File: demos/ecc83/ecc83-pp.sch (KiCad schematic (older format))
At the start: 15 parts, among them P1 IN, P2 OUT, P3 POWER, P4 CONN_2, P5 CONN_1, P6 CONN_1, P7 CONN_1, P8 CONN_1, U1 ECC83

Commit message: Update demos to use sym-lib-table and recent libraries
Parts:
- C1, C2: symbol C -> ecc83_schlib:C
- P1, P2, P3, P4: symbol CONN_2 -> ecc83_schlib:CONN_2
- P5, P6, P7, P8: symbol CONN_1 -> ecc83_schlib:CONN_1
- R1, R2, R3, R4: symbol R -> ecc83_schlib:R
- U1: symbol ECC83 -> ecc83_schlib:ECC83
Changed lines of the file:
@@
-EESchema Schematic File Version 2
-LIBS:ecc83_schlib
-EELAYER 25 0
+EESchema Schematic File Version 4
+LIBS:ecc83-pp-cache
+EELAYER 26 0
 EELAYER END
 $Descr A4 11693 8268
@@
 	6200 3500 6200 3850
 $Comp
-L ECC83 U1
+L ecc83_schlib:ECC83 U1
 U 3 1 48B4F266
 P 2500 2950
@@
 $EndComp
 $Comp
-L ECC83 U1
+L ecc83_schlib:ECC83 U1
 U 2 1 48B4F263
 P 6200 4250
@@
 $EndComp
 $Comp
-L ECC83 U1
+L ecc83_schlib:ECC83 U1
 U 1 1 48B4F256
 P 6300 2550
@@
 $EndComp
 $Comp
-L GND #PWR01
+L ecc83_schlib:GND #PWR01
 U 1 1 457DBAF8
 P 7700 3300
@@
 $EndComp
 $Comp
-L GND #PWR02
+L ecc83_schlib:GND #PWR02
 U 1 1 457DBAF5
 P 7300 3550
@@
 $EndComp
 $Comp
-L GND #PWR03
+L ecc83_schlib:GND #PWR03
 U 1 1 457DBAF1
 P 6100 5200
@@
 $EndComp
 $Comp
-L GND #PWR04
+L ecc83_schlib:GND #PWR04
 U 1 1 457DBAEF
 P 5700 5200
@@
 $EndComp
 $Comp
-L PWR_FLAG #FLG05
+L ecc83_schlib:PWR_FLAG #FLG05
 U 1 1 457DBAC0
 P 3000 2350
@@
 $EndComp
 $Comp
-L CONN_2 P4
+L ecc83_schlib:CONN_2 P4
 U 1 1 456A8ACC
 P 1650 3600
@@
 $EndComp
 $Comp
-L C C1
+L ecc83_schlib:C C1
 U 1 1 4549F4BE
 P 3400 2250
@@
 $EndComp
 $Comp
-L CONN_2 P3
+L ecc83_schlib:CONN_2 P3
 U 1 1 4549F4A5
 P 1650 2100
@@
 $EndComp
 $Comp
-L CONN_2 P2
+L ecc83_schlib:CONN_2 P2
 U 1 1 4549F46C
 P 8150 3100
@@
 $EndComp
 $Comp
-L CONN_2 P1
+L ecc83_schlib:CONN_2 P1
 U 1 1 4549F464
 P 5000 4350
@@
 $EndComp
 $Comp
-L C C2
+L ecc83_schlib:C C2
 U 1 1 4549F3BE
 P 6900 3000
@@
 $EndComp
 $Comp
-L R R3
+L ecc83_schlib:R R3
 U 1 1 4549F3AD
 P 7300 3350
@@
 $EndComp
 $Comp
-L R R4
+L ecc83_schlib:R R4
 U 1 1 4549F3A2
 P 5700 5000
@@
 $EndComp
 $Comp
-L R R2
+L ecc83_schlib:R R2
 U 1 1 4549F39D
 P 6100 5000
@@
 $EndComp
 $Comp
-L R R1
+L ecc83_schlib:R R1
 U 1 1 4549F38A
 P 6200 3350
@@
 $EndComp
 $Comp
-L GND #PWR06
+L ecc83_schlib:GND #PWR06
 U 1 1 53B6F370
 P 3400 2450
@@
 $EndComp
 $Comp
-L CONN_1 P5
+L ecc83_schlib:CONN_1 P5
 U 1 1 54A5890A
 P 6250 7000
@@
 $EndComp
 $Comp
-L CONN_1 P6
+L ecc83_schlib:CONN_1 P6
 U 1 1 54A58C65
 P 6250 7100
@@
 $EndComp
 $Comp
-L CONN_1 P7
+L ecc83_schlib:CONN_1 P7
 U 1 1 54A58C8A
 P 6250 7200
@@
 $EndComp
 $Comp
-L CONN_1 P8
+L ecc83_schlib:CONN_1 P8
 U 1 1 54A58CA3
 P 6250 7300
@@
 	3400 2450 3400 2400
 $Comp
-L PWR_FLAG #FLG07
+L ecc83_schlib:PWR_FLAG #FLG07
 U 1 1 550EA992
 P 3000 1950
@@
 Connection ~ 3000 2000
 $Comp
-L GND #PWR08
+L ecc83_schlib:GND #PWR08
 U 1 1 550EAB37
 P 3000 2550
@@
 Connection ~ 3000 2450
 $Comp
-L GND #PWR09
+L ecc83_schlib:GND #PWR09
 U 1 1 550EAF5A
 P 5450 4600

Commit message: update demo ecc83
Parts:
- C1: symbol ecc83_schlib:C -> ecc83_schlib:CP
- P1, P2, P3, P4: footprint connect:bornier2 -> TerminalBlock_Phoenix:TerminalBlock_Phoenix_MKDS-1,5-2_1x02_P5.00mm_Horizontal
- U1: footprint Valves:VALVE-ECC-83-1 -> Valve:Valve_ECC-83-1
- U1: footprint Valves:VALVE-ECC-83-1 -> (none)
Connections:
- net at U1.4 (F1), U1.5 (F1): now also P4.2 (PM); no longer P4.1 (P1)
- net at U1.9 (F2): now also P4.1 (P1); no longer P4.2 (PM)
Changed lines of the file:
@@
 	6100 4650 6100 4850
 Wire Wire Line
-	2000 2000 6300 2000
+	2000 2000 3000 2000
 Connection ~ 3400 2000
 Wire Wire Line
-	7050 3000 7800 3000
+	7050 3000 7300 3000
 Wire Wire Line
 	7300 3000 7300 3200
 Wire Wire Line
-	2000 3500 2600 3500
+	2000 3500 2400 3500
 Wire Wire Line
 	2400 3500 2400 3400
 Wire Wire Line
-	6200 3500 6200 3850
+	6200 3500 6200 3700
 $Comp
 L ecc83_schlib:ECC83 U1
@@
 F 0 "U1" H 2500 3400 50  0000 C CNN
 F 1 "ECC83" H 2500 3300 50  0000 C CNN
-F 2 "Valves:VALVE-ECC-83-1" V 2250 2950 30  0000 C CNN
+F 2 "" V 2250 2950 30  0000 C CNN
 F 3 "" H 2500 2950 60  0001 C CNN
 	3    2500 2950
@@
 F 0 "U1" H 6350 4600 50  0000 C CNN
 F 1 "ECC83" H 6400 3900 50  0000 C CNN
-F 2 "Valves:VALVE-ECC-83-1" H 6400 3850 30  0000 C CNN
+F 2 "" H 6400 3850 30  0000 C CNN
 F 3 "" H 6200 4250 60  0001 C CNN
 	2    6200 4250
@@
 F 0 "U1" H 6450 2900 50  0000 C CNN
 F 1 "ECC83" H 6050 2250 50  0000 C CNN
-F 2 "Valves:VALVE-ECC-83-1" H 6570 2150 50  0001 C CNN
+F 2 "Valve:Valve_ECC-83-1" V 6550 2550 30  0000 C CNN
 F 3 "" H 6300 2550 60  0001 C CNN
 	1    6300 2550
@@
 L ecc83_schlib:PWR_FLAG #FLG05
 U 1 1 457DBAC0
-P 3000 2350
-F 0 "#FLG05" H 3000 2620 30  0001 C CNN
-F 1 "PWR_FLAG" H 3000 2580 30  0000 C CNN
-F 2 "" H 3000 2350 60  0001 C CNN
-F 3 "" H 3000 2350 60  0001 C CNN
-	1    3000 2350
-	1    0    0    -1
+P 2100 2200
+F 0 "#FLG05" H 2100 2470 30  0001 C CNN
+F 1 "PWR_FLAG" H 2100 2430 30  0000 C CNN
+F 2 "" H 2100 2200 60  0001 C CNN
+F 3 "" H 2100 2200 60  0001 C CNN
+	1    2100 2200
+	0    1    1    0
 $EndComp
 $Comp
@@
 F 0 "P4" V 1600 3600 40  0000 C CNN
 F 1 "CONN_2" V 1700 3600 40  0000 C CNN
-F 2 "connect:bornier2" H 1650 3600 60  0001 C CNN
+F 2 "TerminalBlock_Phoenix:TerminalBlock_Phoenix_MKDS-1,5-2_1x02_P5.00mm_Horizontal" H 1600 3800 15  0000 C CNN
 F 3 "" H 1650 3600 60  0001 C CNN
 	1    1650 3600
-	-1   0    0    -1
-$EndComp
-$Comp
-L ecc83_schlib:C C1
+	-1   0    0    1
+$EndComp
+$Comp
+L ecc83_schlib:CP C1
 U 1 1 4549F4BE
 P 3400 2250
-F 0 "C1" H 3450 2350 50  0000 L CNN
-F 1 "10uF" H 3150 2350 50  0000 L CNN
-F 2 "discret:C2V10" H 3400 2250 60  0001 C CNN
+F 0 "C1" H 3150 2300 50  0000 L CNN
+F 1 "10uF" H 3100 2200 50  0000 L CNN
+F 2 "discret:C2V10" H 3200 2150 30  0000 C CNN
 F 3 "" H 3400 2250 60  0001 C CNN
 	1    3400 2250
@@
 U 1 1 4549F4A5
 P 1650 2100
-F 0 "P3" V 1600 2100 40  0000 C CNN
+F 0 "P3" H 1650 2300 40  0000 C CNN
 F 1 "POWER" V 1700 2100 40  0000 C CNN
-F 2 "connect:bornier2" H 1650 2100 60  0001 C CNN
+F 2 "TerminalBlock_Phoenix:TerminalBlock_Phoenix_MKDS-1,5-2_1x02_P5.00mm_Horizontal" H 1650 1900 15  0000 C CNN
 F 3 "" H 1650 2100 60  0001 C CNN
 	1    1650 2100
@@
 U 1 1 4549F46C
 P 8150 3100
-F 0 "P2" V 8100 3100 40  0000 C CNN
+F 0 "P2" H 8150 3300 40  0000 C CNN
 F 1 "OUT" V 8200 3100 40  0000 C CNN
-F 2 "connect:bornier2" H 8150 3100 60  0001 C CNN
+F 2 "TerminalBlock_Phoenix:TerminalBlock_Phoenix_MKDS-1,5-2_1x02_P5.00mm_Horizontal" H 8150 2900 15  0000 C CNN
 F 3 "" H 8150 3100 60  0001 C CNN
 	1    8150 3100
@@
 U 1 1 4549F464
 P 5000 4350
-F 0 "P1" V 4950 4350 40  0000 C CNN
-F 1 "IN" V 5050 4350 40  0000 C CNN
-F 2 "connect:bornier2" H 5000 4600 50  0000 C CNN
+F 0 "P1" H 5000 4150 40  0000 C CNN
+F 1 "IN" H 5000 4350 40  0000 C CNN
+F 2 "TerminalBlock_Phoenix:TerminalBlock_Phoenix_MKDS-1,5-2_1x02_P5.00mm_Horizontal" H 5000 4550 15  0000 C CNN
 F 3 "" H 5000 4350 60  0001 C CNN
 	1    5000 4350
@@
 F 0 "C2" V 6750 3000 50  0000 C CNN
 F 1 "680nF" V 7050 3000 50  0000 C CNN
-F 2 "discret:C2" H 6900 3000 60  0001 C CNN
+F 2 "discret:C2" V 7100 3000 30  0000 C CNN
 F 3 "" H 6900 3000 60  0001 C CNN
 	1    6900 3000
@@
 U 1 1 4549F3AD
 P 7300 3350
-F 0 "R3" H 7200 3550 50  0000 C CNN
+F 0 "R3" H 7200 3350 50  0000 C CNN
 F 1 "100K" V 7300 3350 50  0000 C CNN
-F 2 "discret:R3" H 7300 3350 60  0001 C CNN
+F 2 "discret:R3" V 7379 3350 30  0000 C CNN
 F 3 "" H 7300 3350 60  0001 C CNN
 	1    7300 3350
@@
 U 1 1 4549F3A2
 P 5700 5000
-F 0 "R4" H 5600 5200 50  0000 C CNN
+F 0 "R4" H 5600 5050 50  0000 C CNN
 F 1 "47K" V 5700 5000 50  0000 C CNN
-F 2 "discret:R3" H 5700 5000 60  0001 C CNN
+F 2 "discret:R3" V 5776 4998 30  0000 C CNN
 F 3 "" H 5700 5000 60  0001 C CNN
 	1    5700 5000
@@
 U 1 1 4549F39D
 P 6100 5000
-F 0 "R2" H 6000 5200 50  0000 C CNN
+F 0 "R2" H 6000 5000 50  0000 C CNN
 F 1 "1.5K" V 6100 5000 50  0000 C CNN
-F 2 "discret:R3" H 6100 5000 60  0001 C CNN
+F 2 "discret:R3" V 6174 5000 30  0000 C CNN
 F 3 "" H 6100 5000 60  0001 C CNN
 	1    6100 5000
@@
 U 1 1 4549F38A
 P 6200 3350
-F 0 "R1" H 6300 3150 50  0000 C CNN
+F 0 "R1" H 6300 3350 50  0000 C CNN
 F 1 "1.5K" V 6200 3350 50  0000 C CNN
-F 2 "discret:R3" H 6200 3350 60  0001 C CNN
+F 2 "discret:R3" V 6120 3348 30  0000 C CNN
 F 3 "" H 6200 3350 60  0001 C CNN
 	1    6200 3350
@@
 	2600 3500 2600 3400
 Wire Wire Line
-	5350 4250 5900 4250
+	5350 4250 5700 4250
 Wire Wire Line
 	5700 4250 5700 4850
 Connection ~ 5700 4250
 Wire Wire Line
-	6200 2950 6200 3200
+	6200 2950 6200 3000
 Connection ~ 6200 3700
 Wire Wire Line
@@
 L ecc83_schlib:GND #PWR08
 U 1 1 550EAB37
-P 3000 2550
-F 0 "#PWR08" H 3000 2550 30  0001 C CNN
-F 1 "GND" H 3000 2480 30  0001 C CNN
-F 2 "" H 3000 2550 60  0001 C CNN
-F 3 "" H 3000 2550 60  0001 C CNN
-	1    3000 2550
+P 2000 2250
+F 0 "#PWR08" H 2000 2250 30  0001 C CNN
+F 1 "GND" H 2000 2180 30  0001 C CNN
+F 2 "" H 2000 2250 60  0001 C CNN
+F 3 "" H 2000 2250 60  0001 C CNN
+	1    2000 2250
 	-1   0    0    -1
 $EndComp
-Wire Wire Line
-	3000 2350 3000 2550
-Wire Wire Line
-	2000 2200 2800 2200
-Wire Wire Line
-	2800 2200 2800 2450
-Wire Wire Line
-	2800 2450 3000 2450
-Connection ~ 3000 2450
 $Comp
 L ecc83_schlib:GND #PWR09
@@
 NoConn ~ 6100 7200
 NoConn ~ 6100 7300
+Wire Wire Line
+	3400 2000 6300 2000
+Wire Wire Line
+	2400 3500 2600 3500
+Wire Wire Line
+	5700 4250 5900 4250
+Wire Wire Line
+	6200 3700 6200 3850
+Wire Wire Line
+	7300 3000 7800 3000
+Wire Wire Line
+	6200 3000 6200 3200
+Wire Wire Line
+	3000 2000 3400 2000
+Wire Wire Line
+	2100 2200 2000 2200
+Wire Wire Line
+	2000 2250 2000 2200
 $EndSCHEMATC

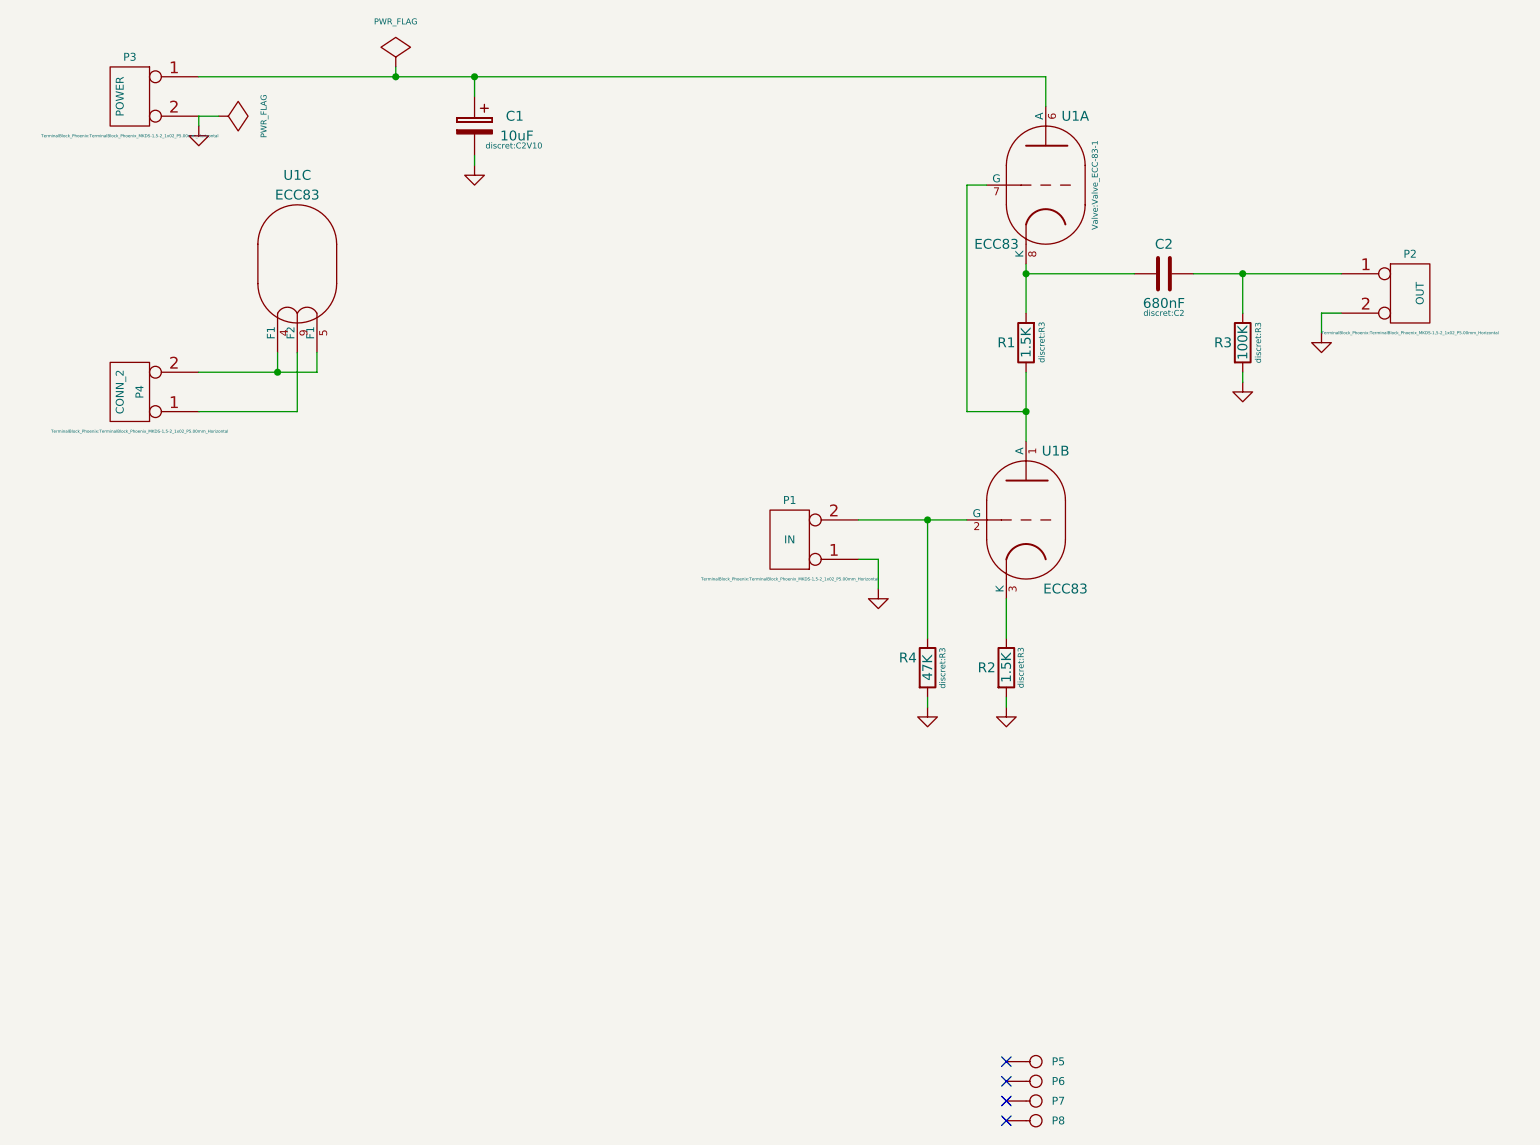
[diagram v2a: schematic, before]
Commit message: Update ecc83 demo
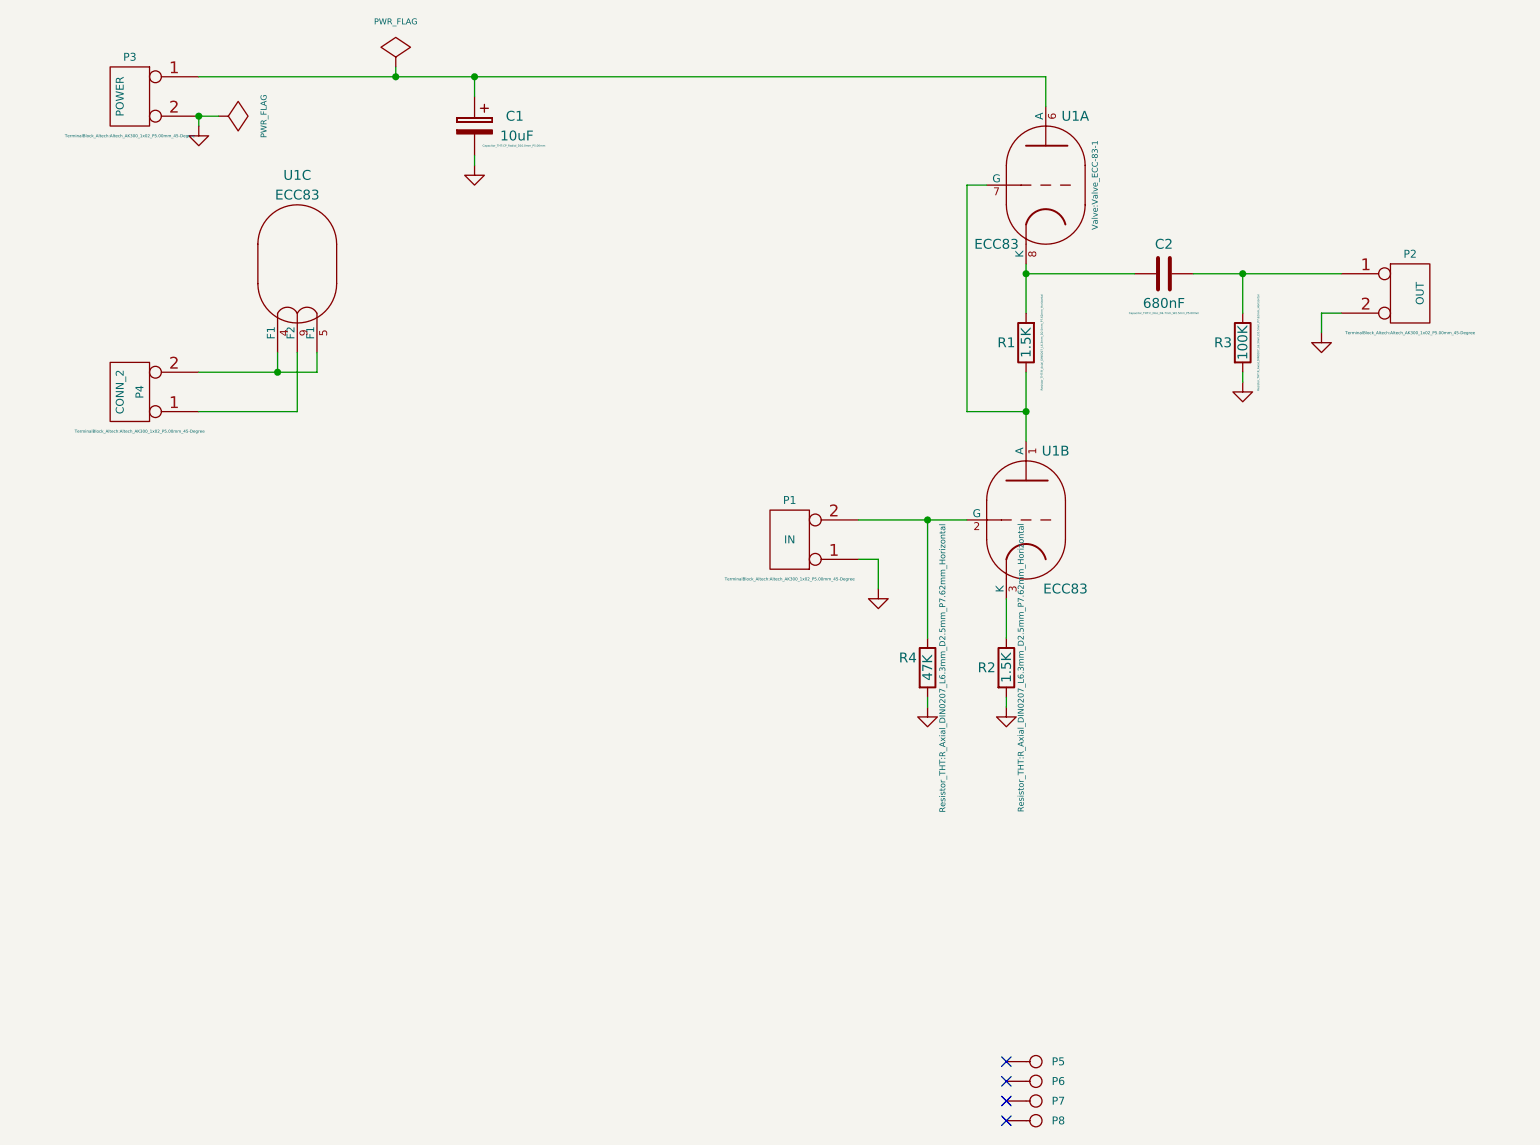
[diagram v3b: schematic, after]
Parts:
- C1: footprint discret:C2V10 -> Capacitor_THT:CP_Radial_D10.0mm_P5.00mm
- C2: footprint discret:C2 -> Capacitor_THT:C_Disc_D4.7mm_W2.5mm_P5.00mm
- P1, P2, P3, P4: footprint TerminalBlock_Phoenix:TerminalBlock_Phoenix_MKDS-1,5-2_1x02_P5.00mm_Horizontal -> TerminalBlock_Altech:Altech_AK300_1x02_P5.00mm_45-Degree
- P5, P6, P7, P8: value CONN_1 -> MOUNTING_HOLE; footprint connect:1pin -> MountingHole:MountingHole_3.2mm_M3_DIN965_Pad
- R1, R2, R3, R4: footprint discret:R3 -> Resistor_THT:R_Axial_DIN0207_L6.3mm_D2.5mm_P7.62mm_Horizontal
- U1: footprint (none) -> Valve:Valve_ECC-83-1
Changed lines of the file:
@@
-EESchema Schematic File Version 4
-LIBS:ecc83-pp-cache
-EELAYER 26 0
+EESchema Schematic File Version 5
+EELAYER 30 0
 EELAYER END
 $Descr A4 11693 8268
@@
 Comment3 ""
 Comment4 ""
+Comment5 ""
+Comment6 ""
+Comment7 ""
+Comment8 ""
+Comment9 ""
 $EndDescr
 Wire Wire Line
@@
 F 0 "U1" H 2500 3400 50  0000 C CNN
 F 1 "ECC83" H 2500 3300 50  0000 C CNN
-F 2 "" V 2250 2950 30  0000 C CNN
+F 2 "Valve:Valve_ECC-83-1" V 2250 2950 30  0001 C CNN
 F 3 "" H 2500 2950 60  0001 C CNN
 	3    2500 2950
@@
 F 0 "U1" H 6350 4600 50  0000 C CNN
 F 1 "ECC83" H 6400 3900 50  0000 C CNN
-F 2 "" H 6400 3850 30  0000 C CNN
+F 2 "Valve:Valve_ECC-83-1" H 6400 3850 30  0001 C CNN
 F 3 "" H 6200 4250 60  0001 C CNN
 	2    6200 4250
@@
 F 0 "P4" V 1600 3600 40  0000 C CNN
 F 1 "CONN_2" V 1700 3600 40  0000 C CNN
-F 2 "TerminalBlock_Phoenix:TerminalBlock_Phoenix_MKDS-1,5-2_1x02_P5.00mm_Horizontal" H 1600 3800 15  0000 C CNN
+F 2 "TerminalBlock_Altech:Altech_AK300_1x02_P5.00mm_45-Degree" H 1600 3800 15  0000 C CNN
 F 3 "" H 1650 3600 60  0001 C CNN
 	1    1650 3600
@@
 F 0 "C1" H 3150 2300 50  0000 L CNN
 F 1 "10uF" H 3100 2200 50  0000 L CNN
-F 2 "discret:C2V10" H 3200 2150 30  0000 C CNN
+F 2 "Capacitor_THT:CP_Radial_D10.0mm_P5.00mm" H 3200 2150 10  0000 C CNN
 F 3 "" H 3400 2250 60  0001 C CNN
 	1    3400 2250
@@
 F 0 "P3" H 1650 2300 40  0000 C CNN
 F 1 "POWER" V 1700 2100 40  0000 C CNN
-F 2 "TerminalBlock_Phoenix:TerminalBlock_Phoenix_MKDS-1,5-2_1x02_P5.00mm_Horizontal" H 1650 1900 15  0000 C CNN
+F 2 "TerminalBlock_Altech:Altech_AK300_1x02_P5.00mm_45-Degree" H 1650 1900 15  0000 C CNN
 F 3 "" H 1650 2100 60  0001 C CNN
 	1    1650 2100
@@
 F 0 "P2" H 8150 3300 40  0000 C CNN
 F 1 "OUT" V 8200 3100 40  0000 C CNN
-F 2 "TerminalBlock_Phoenix:TerminalBlock_Phoenix_MKDS-1,5-2_1x02_P5.00mm_Horizontal" H 8150 2900 15  0000 C CNN
+F 2 "TerminalBlock_Altech:Altech_AK300_1x02_P5.00mm_45-Degree" H 8150 2900 15  0000 C CNN
 F 3 "" H 8150 3100 60  0001 C CNN
 	1    8150 3100
@@
 F 0 "P1" H 5000 4150 40  0000 C CNN
 F 1 "IN" H 5000 4350 40  0000 C CNN
-F 2 "TerminalBlock_Phoenix:TerminalBlock_Phoenix_MKDS-1,5-2_1x02_P5.00mm_Horizontal" H 5000 4550 15  0000 C CNN
+F 2 "TerminalBlock_Altech:Altech_AK300_1x02_P5.00mm_45-Degree" H 5000 4550 15  0000 C CNN
 F 3 "" H 5000 4350 60  0001 C CNN
 	1    5000 4350
@@
 F 0 "C2" V 6750 3000 50  0000 C CNN
 F 1 "680nF" V 7050 3000 50  0000 C CNN
-F 2 "discret:C2" V 7100 3000 30  0000 C CNN
+F 2 "Capacitor_THT:C_Disc_D4.7mm_W2.5mm_P5.00mm" V 7100 3000 10  0000 C CNN
 F 3 "" H 6900 3000 60  0001 C CNN
 	1    6900 3000
@@
 F 0 "R3" H 7200 3350 50  0000 C CNN
 F 1 "100K" V 7300 3350 50  0000 C CNN
-F 2 "discret:R3" V 7379 3350 30  0000 C CNN
+F 2 "Resistor_THT:R_Axial_DIN0207_L6.3mm_D2.5mm_P7.62mm_Horizontal" V 7379 3350 10  0000 C CNN
 F 3 "" H 7300 3350 60  0001 C CNN
 	1    7300 3350
@@
 F 0 "R4" H 5600 5050 50  0000 C CNN
 F 1 "47K" V 5700 5000 50  0000 C CNN
-F 2 "discret:R3" V 5776 4998 30  0000 C CNN
+F 2 "Resistor_THT:R_Axial_DIN0207_L6.3mm_D2.5mm_P7.62mm_Horizontal" V 5776 4998 30  0000 C CNN
 F 3 "" H 5700 5000 60  0001 C CNN
 	1    5700 5000
@@
 F 0 "R2" H 6000 5000 50  0000 C CNN
 F 1 "1.5K" V 6100 5000 50  0000 C CNN
-F 2 "discret:R3" V 6174 5000 30  0000 C CNN
+F 2 "Resistor_THT:R_Axial_DIN0207_L6.3mm_D2.5mm_P7.62mm_Horizontal" V 6174 5000 30  0000 C CNN
 F 3 "" H 6100 5000 60  0001 C CNN
 	1    6100 5000
@@
 F 0 "R1" H 6300 3350 50  0000 C CNN
 F 1 "1.5K" V 6200 3350 50  0000 C CNN
-F 2 "discret:R3" V 6120 3348 30  0000 C CNN
+F 2 "Resistor_THT:R_Axial_DIN0207_L6.3mm_D2.5mm_P7.62mm_Horizontal" V 6120 3348 10  0000 C CNN
 F 3 "" H 6200 3350 60  0001 C CNN
 	1    6200 3350
@@
 $EndComp
 $Comp
-L ecc83_schlib:CONN_1 P5
-U 1 1 54A5890A
-P 6250 7000
-F 0 "P5" H 6330 7000 40  0000 L CNN
-F 1 "CONN_1" H 6250 7055 30  0001 C CNN
-F 2 "connect:1pin" H 6250 7000 60  0001 C CNN
-F 3 "" H 6250 7000 60  0000 C CNN
-	1    6250 7000
-	1    0    0    -1
-$EndComp
-$Comp
 L ecc83_schlib:CONN_1 P6
 U 1 1 54A58C65
 P 6250 7100
 F 0 "P6" H 6330 7100 40  0000 L CNN
-F 1 "CONN_1" H 6250 7155 30  0001 C CNN
-F 2 "connect:1pin" H 6250 7100 60  0001 C CNN
+F 1 "MOUNTING_HOLE" H 6250 7155 30  0001 C CNN
+F 2 "MountingHole:MountingHole_3.2mm_M3_DIN965_Pad" H 6250 7100 60  0001 C CNN
 F 3 "" H 6250 7100 60  0000 C CNN
 	1    6250 7100
@@
 P 6250 7200
 F 0 "P7" H 6330 7200 40  0000 L CNN
-F 1 "CONN_1" H 6250 7255 30  0001 C CNN
-F 2 "connect:1pin" H 6250 7200 60  0001 C CNN
+F 1 "MOUNTING_HOLE" H 6250 7255 30  0001 C CNN
+F 2 "MountingHole:MountingHole_3.2mm_M3_DIN965_Pad" H 6250 7200 60  0001 C CNN
 F 3 "" H 6250 7200 60  0000 C CNN
 	1    6250 7200
@@
 P 6250 7300
 F 0 "P8" H 6330 7300 40  0000 L CNN
-F 1 "CONN_1" H 6250 7355 30  0001 C CNN
-F 2 "connect:1pin" H 6250 7300 60  0001 C CNN
+F 1 "MOUNTING_HOLE" H 6250 7355 30  0001 C CNN
+F 2 "MountingHole:MountingHole_3.2mm_M3_DIN965_Pad" H 6250 7300 60  0001 C CNN
 F 3 "" H 6250 7300 60  0000 C CNN
 	1    6250 7300
@@
 Wire Wire Line
 	2000 2250 2000 2200
+Connection ~ 2000 2200
+$Comp
+L ecc83_schlib:CONN_1 P5
+U 1 1 54A5890A
+P 6250 7000
+F 0 "P5" H 6330 7000 40  0000 L CNN
+F 1 "MOUNTING_HOLE" H 6250 7055 30  0001 C CNN
+F 2 "MountingHole:MountingHole_3.2mm_M3_DIN965_Pad" H 6250 7000 60  0001 C CNN
+F 3 "" H 6250 7000 60  0000 C CNN
+	1    6250 7000
+	1    0    0    -1
+$EndComp
 $EndSCHEMATC
